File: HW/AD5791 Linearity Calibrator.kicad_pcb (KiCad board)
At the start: 4 copper layers, 80 x 100 mm, 67 parts, among them J10 PWR, J11 PWR, J12 PWR, J13 PWR, J2 VREFP, J3 VREFN, J5 VREFP, J6 SIG, J7 PWR, J8 VREFN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

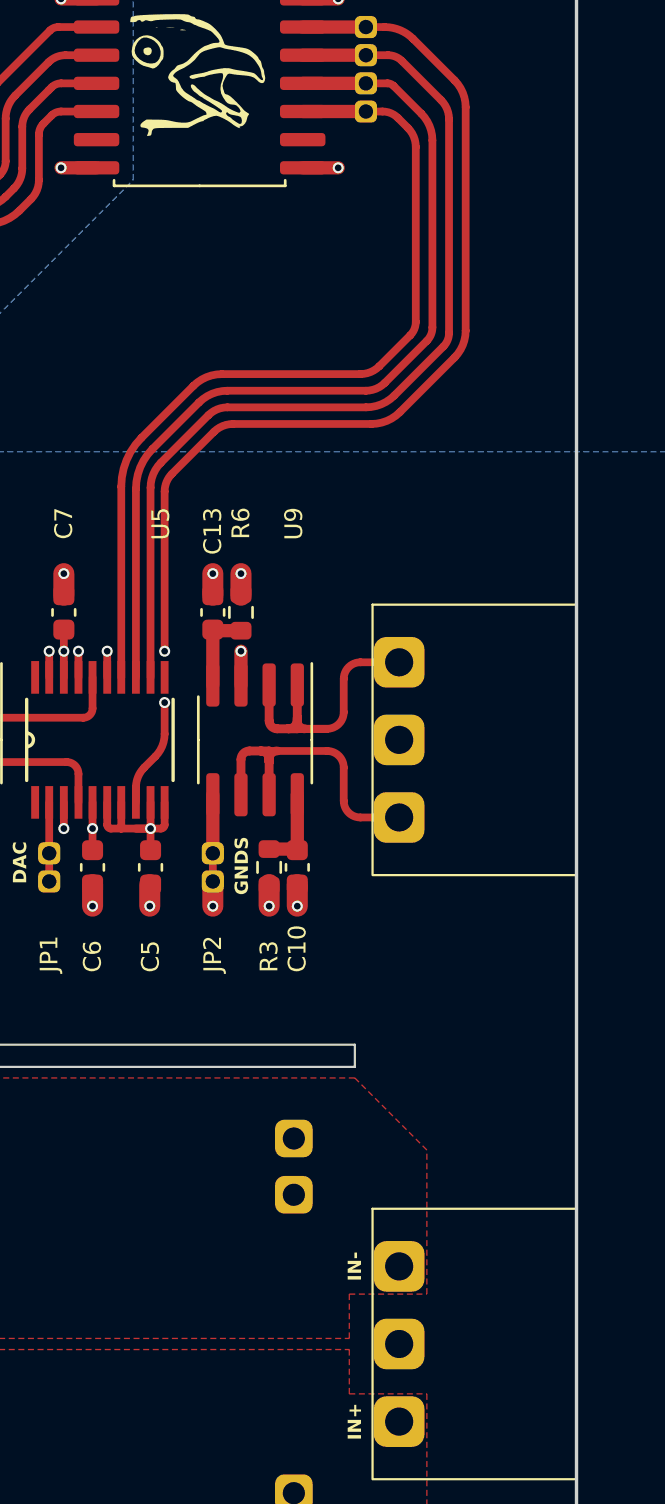
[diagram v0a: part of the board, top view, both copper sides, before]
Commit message: added net and silkscreen labels
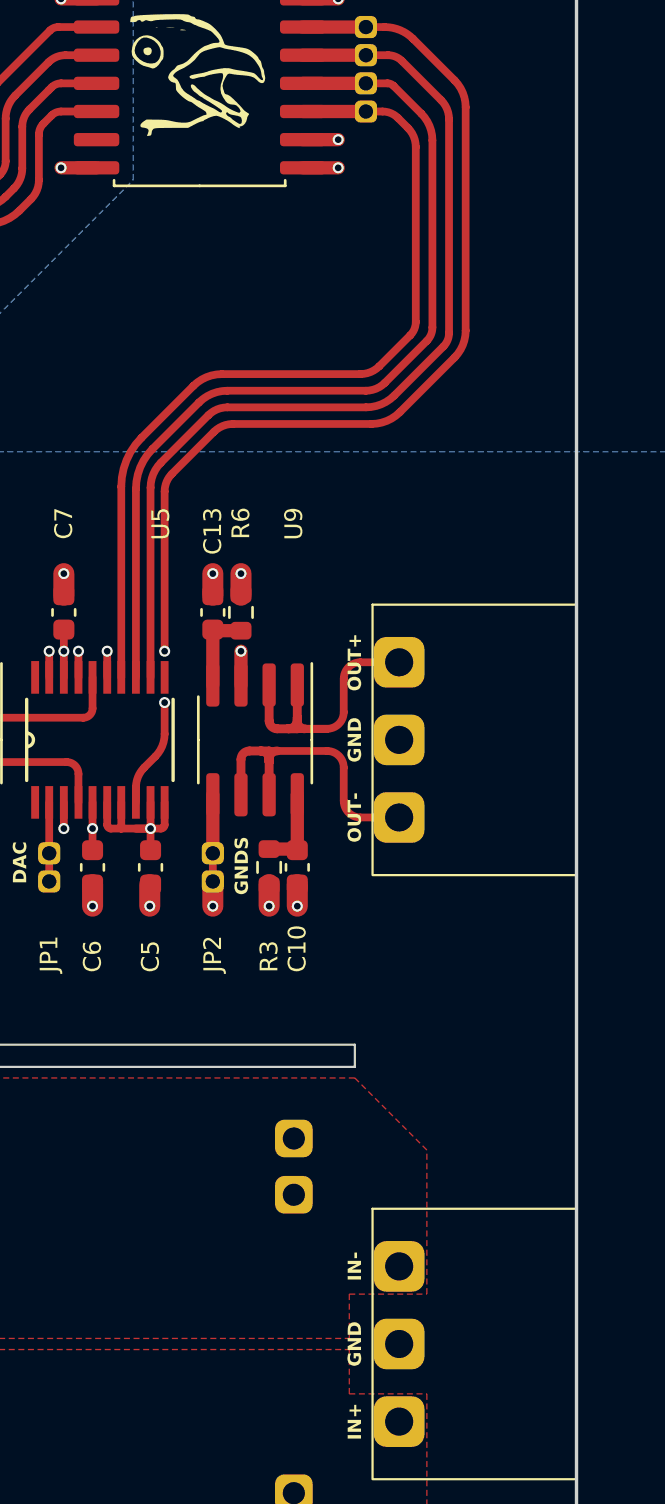
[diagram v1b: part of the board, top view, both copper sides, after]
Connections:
- net Net-(J4-Pin_1) renamed /OUT+
- net Net-(J4-Pin_3) renamed /OUT-
- U13 pad 10: unconnected-(U13-VE2-Pad10) -> +3.3V
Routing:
- net +3.3V: track 11.6 -> 13.2 mm, vias 2 -> 3
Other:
- board text added: "OUT+"
- board text added: "OUT-"

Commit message: fixed small PCB mistake
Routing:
- net /BUFIN: track 23.6 -> 26.3 mm
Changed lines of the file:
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@@
   (segment (start 134.865 98) (end 134.865 99.525) (width 0.6) (layer "F.Cu") (net 65))
   (via (at 134.865 98) (size 0.5) (drill 0.3) (layers "F.Cu" "B.Cu") (net 65))
-  (segment (start 132.951712 102.355788) (end 134.52875 100.77875) (width 0.5) (layer "In1.Cu") (net 65))
-  (segment (start 126.5396 104.5396) (end 127.9146 103.1646) (width 0.5) (layer "In1.Cu") (net 65))
-  (segment (start 134.865 99.966971) (end 134.865 98) (width 0.5) (layer "In1.Cu") (net 65))
-  (segment (start 126.214 107.115) (end 126.214 105.325667) (width 0.5) (layer "In1.Cu") (net 65))
-  (segment (start 128.915532 102.75) (end 132 102.75) (width 0.5) (layer "In1.Cu") (net 65))
-  (arc (start 127.9146 103.1646) (mid 128.373832 102.85775) (end 128.915532 102.75) (width 0.5) (layer "In1.Cu") (net 65))
-  (arc (start 134.52875 100.77875) (mid 134.777611 100.406303) (end 134.865 99.966971) (width 0.5) (layer "In1.Cu") (net 65))
-  (arc (start 126.214 105.325667) (mid 126.298621 104.900251) (end 126.5396 104.5396) (width 0.5) (layer "In1.Cu") (net 65))
-  (arc (start 132 102.75) (mid 132.515064 102.647547) (end 132.951712 102.355788) (width 0.5) (layer "In1.Cu") (net 65))
+  (segment (start 134.52875 100.77875) (end 132.951712 102.355788) (width 0.5) (layer "In1.Cu") (net 65))
+  (segment (start 127.9146 103.1646) (end 125.4146 105.6646) (width 0.5) (layer "In1.Cu") (net 65))
+  (segment (start 125 106.665532) (end 125 108) (width 0.5) (layer "In1.Cu") (net 65))
+  (segment (start 125.385 108.385) (end 126.214 108.385) (width 0.5) (layer "In1.Cu") (net 65))
+  (segment (start 132 102.75) (end 128.915532 102.75) (width 0.5) (layer "In1.Cu") (net 65))
+  (segment (start 134.865 98) (end 134.865 99.966971) (width 0.5) (layer "In1.Cu") (net 65))
+  (arc (start 125 108) (mid 125.112764 108.272236) (end 125.385 108.385) (width 0.5) (layer "In1.Cu") (net 65))
+  (arc (start 128.915532 102.75) (mid 128.373832 102.85775) (end 127.9146 103.1646) (width 0.5) (layer "In1.Cu") (net 65))
+  (arc (start 134.865 99.966971) (mid 134.777611 100.406303) (end 134.52875 100.77875) (width 0.5) (layer "In1.Cu") (net 65))
+  (arc (start 132.951712 102.355788) (mid 132.515064 102.647547) (end 132 102.75) (width 0.5) (layer "In1.Cu") (net 65))
+  (arc (start 125.4146 105.6646) (mid 125.107751 106.123832) (end 125 106.665532) (width 0.5) (layer "In1.Cu") (net 65))
   (segment (start 104.135 104.475) (end 104.135 106.8375) (width 0.6) (layer "F.Cu") (net 66))
   (segment (start 141.5 71.115) (end 137.65 71.115) (width 0.35) (layer "F.Cu") (net 67))

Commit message: minor changes in schem and pcb
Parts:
- J8: value VREFN -> REFCAP
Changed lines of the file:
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@@
         (effects (font (size 0.8 0.8) (thickness 0.15)))
     )
-    (fp_text value "VREFN" (at 0 2.965 135) (layer "F.Fab")
+    (fp_text value "REFCAP" (at 0 2.965 135) (layer "F.Fab")
         (effects (font (size 1 1) (thickness 0.15)))
     )
